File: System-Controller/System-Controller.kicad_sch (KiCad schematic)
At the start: 0 parts

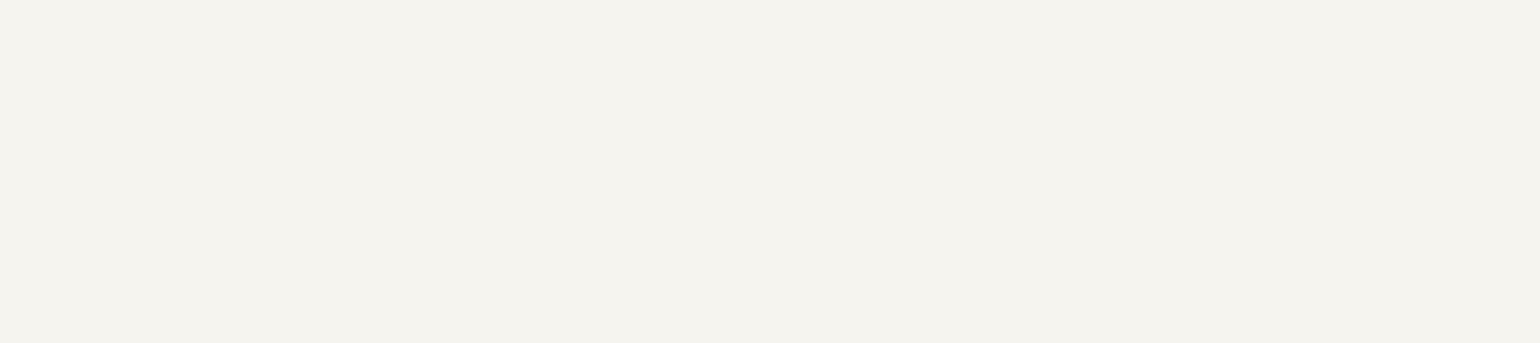
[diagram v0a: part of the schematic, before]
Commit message: Added UVC Project, As-Built version of SystemController.
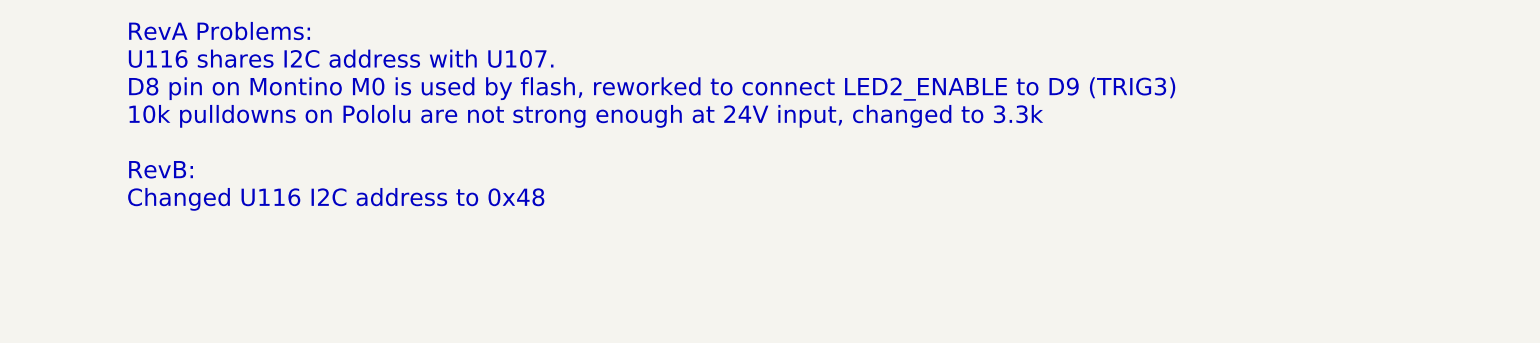
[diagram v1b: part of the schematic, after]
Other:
- note added: "RevA Problems: U116 shares I2C address with U107. D8 pin on Montino M0 is used by flash, reworked to connect LED2_ENABLE to D9 (TRIG3) 10k pulldowns on Pololu are not strong enough at 24V input, changed to 3.3k RevB: Changed U116 I2C address to 0x48"
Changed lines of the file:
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@@
     (rev "B")
+  )
+  (text "RevA Problems:\nU116 shares I2C address with U107. \nD8 pin on Montino M0 is used by flash, reworked to connect LED2_ENABLE to D9 (TRIG3)\n10k pulldowns on Pololu are not strong enough at 24V input, changed to 3.3k\n\nRevB:\nChanged U116 I2C address to 0x48"
+    (at 232.41 48.26 0)
+    (effects (font (size 2.44 2.44)) (justify left bottom))
   )
   (sheet (at 64.77 33.02) (size 68.58 58.42) (fields_autoplaced)
